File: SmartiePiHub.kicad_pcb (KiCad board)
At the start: 2 copper layers, 65 x 56 mm, 10 parts, among them P1 Conn_02x20_Odd_Even

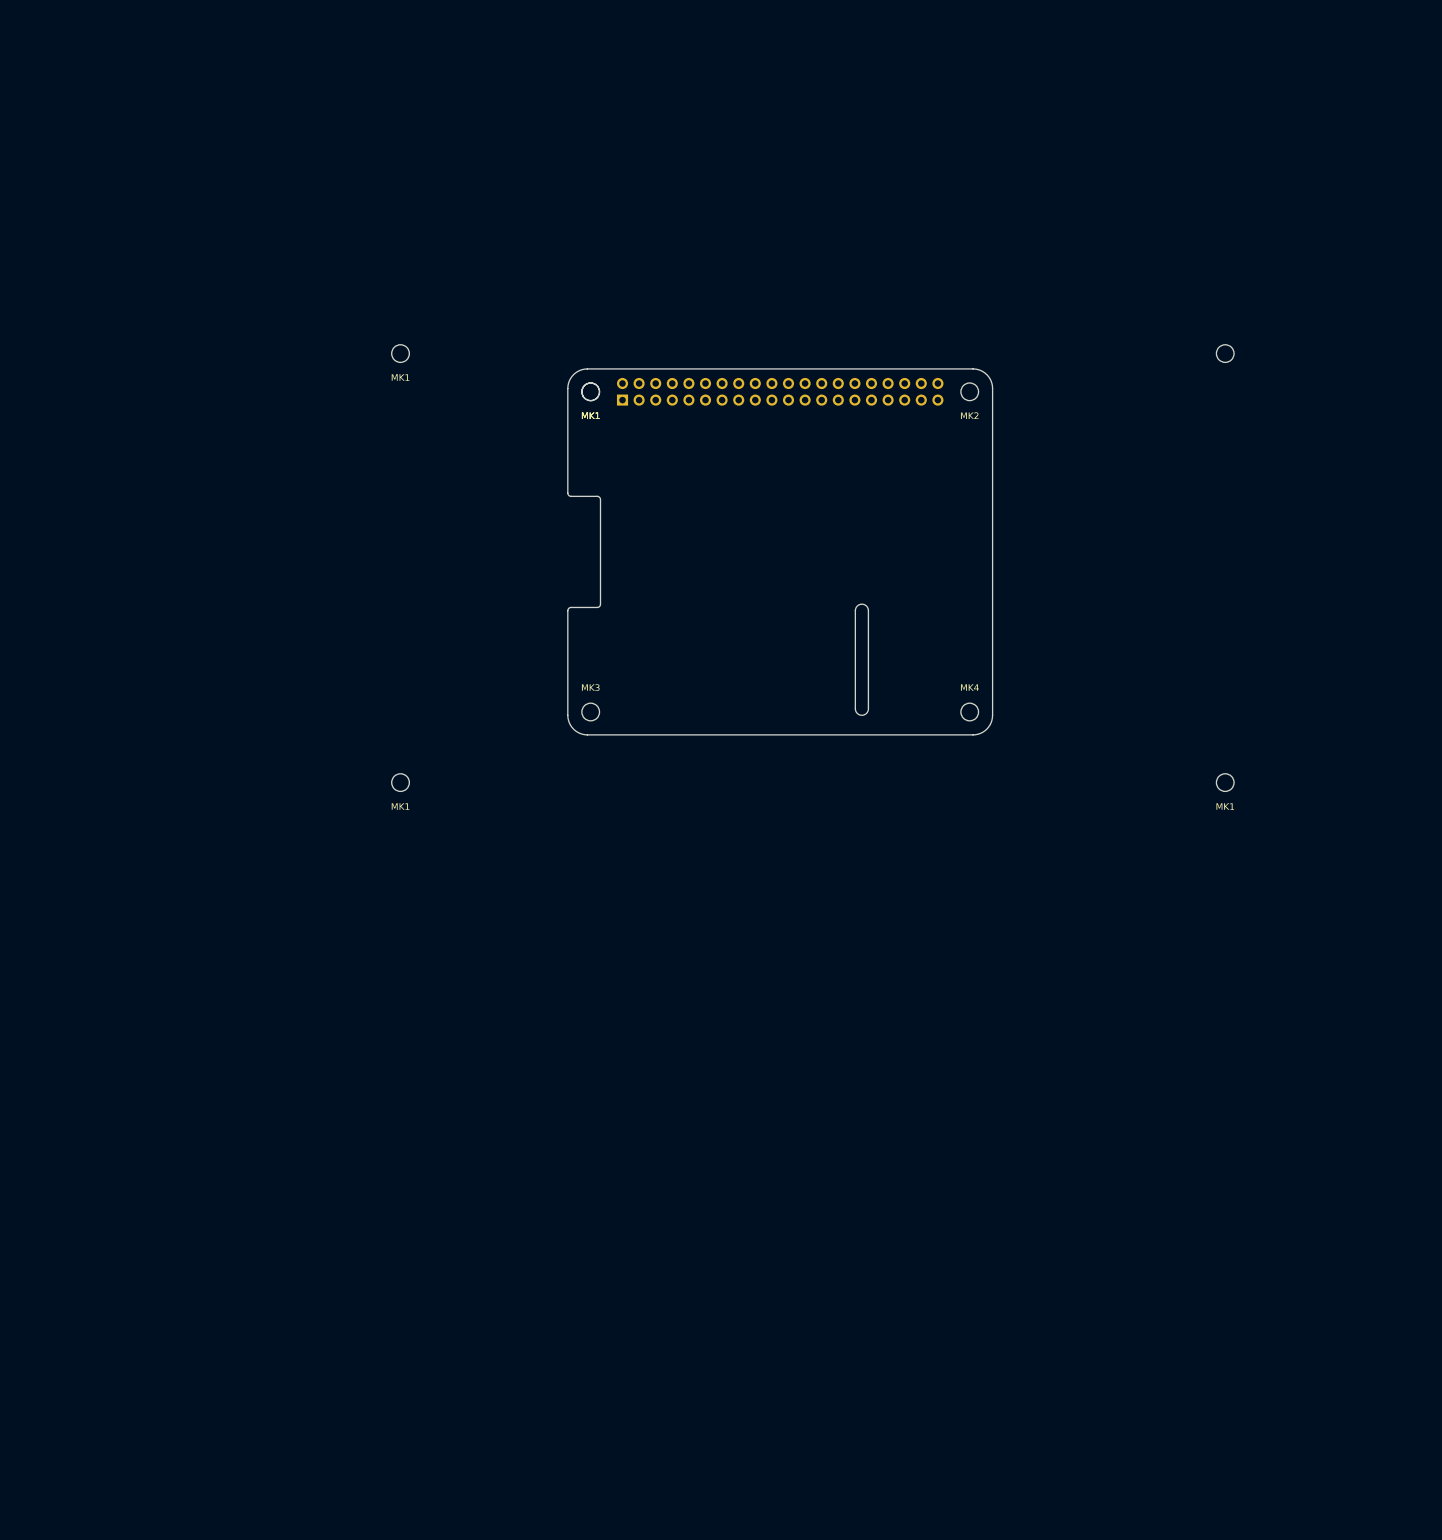
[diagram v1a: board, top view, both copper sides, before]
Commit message: adding more footprints. created netlist
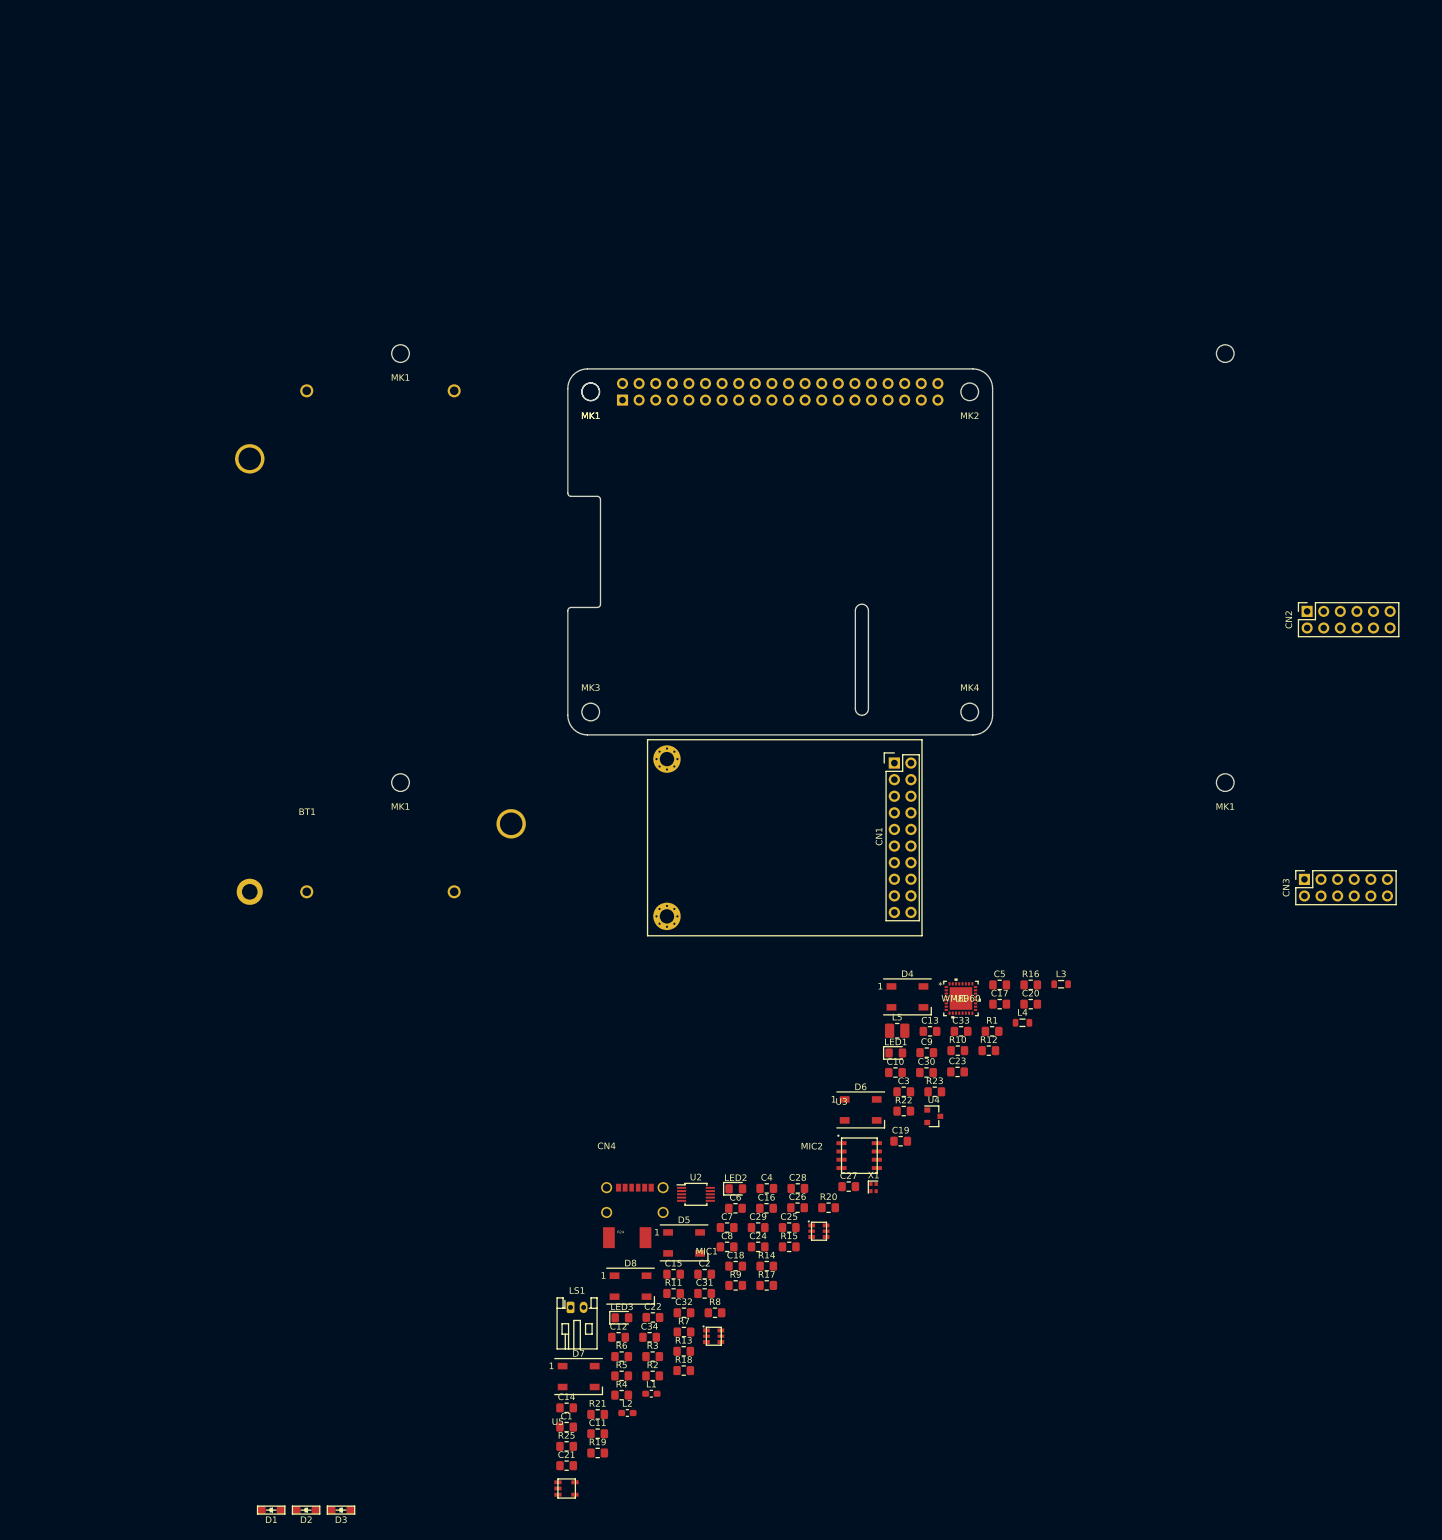
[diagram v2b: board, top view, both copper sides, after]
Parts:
- added BT1: Battery_Cell, SmartiePiHub:KEYSTONE_1123_BATTERY_HOLDER, F.Cu at (160.1, 174.0)
- added C1: 10uF, Capacitor_SMD:C_0805_2012Metric_Pad1.15x1.40mm_HandSolder, F.Cu at (199.8, 255.9)
- added C10: 33pF, Capacitor_SMD:C_0805_2012Metric_Pad1.15x1.40mm_HandSolder, F.Cu at (250.1, 201.7)
- added C11: 33pF, Capacitor_SMD:C_0805_2012Metric_Pad1.15x1.40mm_HandSolder, F.Cu at (204.6, 256.9)
- added C12: 100nF, Capacitor_SMD:C_0805_2012Metric_Pad1.15x1.40mm_HandSolder, F.Cu at (207.8, 242.2)
- added C13: 33pF, Capacitor_SMD:C_0805_2012Metric_Pad1.15x1.40mm_HandSolder, F.Cu at (255.4, 195.4)
- added C14: 33pF, Capacitor_SMD:C_0805_2012Metric_Pad1.15x1.40mm_HandSolder, F.Cu at (199.8, 253.0)
- added C15: 10uF, Capacitor_SMD:C_0805_2012Metric_Pad1.15x1.40mm_HandSolder, F.Cu at (216.2, 232.5)
- added C16: 10uF, Capacitor_SMD:C_0805_2012Metric_Pad1.15x1.40mm_HandSolder, F.Cu at (230.4, 222.4)
- added C17: 10uF, Capacitor_SMD:C_0805_2012Metric_Pad1.15x1.40mm_HandSolder, F.Cu at (266.1, 191.2)
- added C18: .1uF, Capacitor_SMD:C_0805_2012Metric_Pad1.15x1.40mm_HandSolder, F.Cu at (225.7, 231.3)
- added C19: 10uF, Capacitor_SMD:C_0805_2012Metric_Pad1.15x1.40mm_HandSolder, F.Cu at (250.9, 212.2)
- added C2: 10uF, Capacitor_SMD:C_0805_2012Metric_Pad1.15x1.40mm_HandSolder, F.Cu at (220.9, 232.5)
- added C20: .1uF, Capacitor_SMD:C_0805_2012Metric_Pad1.15x1.40mm_HandSolder, F.Cu at (270.8, 191.2)
- added C21: 100pF, Capacitor_SMD:C_0805_2012Metric_Pad1.15x1.40mm_HandSolder, F.Cu at (199.8, 261.8)
- added C22: 10pF, Capacitor_SMD:C_0805_2012Metric_Pad1.15x1.40mm_HandSolder, F.Cu at (213.0, 239.1)
- added C23: DNP, Capacitor_SMD:C_0805_2012Metric_Pad1.15x1.40mm_HandSolder, F.Cu at (259.6, 201.6)
- added C24: 4.7uF, Capacitor_SMD:C_0805_2012Metric_Pad1.15x1.40mm_HandSolder, F.Cu at (229.1, 228.3)
- added C25: .1uF, Capacitor_SMD:C_0805_2012Metric_Pad1.15x1.40mm_HandSolder, F.Cu at (233.9, 225.4)
- added C26: 10uF, Capacitor_SMD:C_0805_2012Metric_Pad1.15x1.40mm_HandSolder, F.Cu at (235.2, 222.4)
- added C27: 10uF, Capacitor_SMD:C_0805_2012Metric_Pad1.15x1.40mm_HandSolder, F.Cu at (243.0, 219.1)
- added C28: 10uF, Capacitor_SMD:C_0805_2012Metric_Pad1.15x1.40mm_HandSolder, F.Cu at (235.2, 219.4)
- added C29: DNP, Capacitor_SMD:C_0805_2012Metric_Pad1.15x1.40mm_HandSolder, F.Cu at (229.1, 225.4)
- added C3: .1uF, Capacitor_SMD:C_0805_2012Metric_Pad1.15x1.40mm_HandSolder, F.Cu at (251.4, 204.6)
- added C30: snub cap, Capacitor_SMD:C_0805_2012Metric_Pad1.15x1.40mm_HandSolder, F.Cu at (254.9, 201.7)
- added C31: 10uF, Capacitor_SMD:C_0805_2012Metric_Pad1.15x1.40mm_HandSolder, F.Cu at (220.9, 235.5)
- added C32: 22uF, Capacitor_SMD:C_0805_2012Metric_Pad1.15x1.40mm_HandSolder, F.Cu at (217.8, 238.4)
- added C33: 10uF, Capacitor_SMD:C_0805_2012Metric_Pad1.15x1.40mm_HandSolder, F.Cu at (260.2, 195.4)
- added C34: DNP, Capacitor_SMD:C_0805_2012Metric_Pad1.15x1.40mm_HandSolder, F.Cu at (212.5, 242.2)
- added C4: .1uF, Capacitor_SMD:C_0805_2012Metric_Pad1.15x1.40mm_HandSolder, F.Cu at (230.4, 219.4)
- added C5: .1uF, Capacitor_SMD:C_0805_2012Metric_Pad1.15x1.40mm_HandSolder, F.Cu at (266.1, 188.3)
- added C6: 10uF, Capacitor_SMD:C_0805_2012Metric_Pad1.15x1.40mm_HandSolder, F.Cu at (225.7, 222.4)
- added C7: .1uF, Capacitor_SMD:C_0805_2012Metric_Pad1.15x1.40mm_HandSolder, F.Cu at (224.4, 225.4)
- added C8: 10uF, Capacitor_SMD:C_0805_2012Metric_Pad1.15x1.40mm_HandSolder, F.Cu at (224.4, 228.3)
- added C9: .1uF, Capacitor_SMD:C_0805_2012Metric_Pad1.15x1.40mm_HandSolder, F.Cu at (254.9, 198.6)
- added CN1: SX1238_TRX_HEADER, SmartiePiHub:sx1238_trx, F.Cu at (250.0, 154.3)
- added CN2: ZIGBEE_TRX_HEADER, Connector_PinSocket_2.54mm:PinSocket_2x06_P2.54mm_Vertical, F.Cu at (313.1, 131.1)
- added CN3: ZWAVE_TRX_HEADER, Connector_PinSocket_2.54mm:PinSocket_2x06_P2.54mm_Vertical, F.Cu at (312.7, 172.1)
- added CN4: USB_C_Plug_USB2.0, SmartiePiHub:USB4125_TYPE_C, F.Cu at (205.9, 219.3)
- added D1: D_Schottky, SmartiePiHub:onsemi-NRVB120VLSFT1G, F.Cu at (154.6, 268.6)
- added D2: D_Schottky, SmartiePiHub:onsemi-NRVB120VLSFT1G, F.Cu at (160.0, 268.6)
- added D3: D_Schottky, SmartiePiHub:onsemi-NRVB120VLSFT1G, F.Cu at (165.3, 268.6)
- added D4: WS2812B, LED_SMD:LED_WS2812B_PLCC4_5.0x5.0mm_P3.2mm, F.Cu at (252.0, 190.1)
- added D5: WS2812B, LED_SMD:LED_WS2812B_PLCC4_5.0x5.0mm_P3.2mm, F.Cu at (217.8, 227.7)
- added D6: WS2812B, LED_SMD:LED_WS2812B_PLCC4_5.0x5.0mm_P3.2mm, F.Cu at (244.8, 207.4)
- added D7: WS2812B, LED_SMD:LED_WS2812B_PLCC4_5.0x5.0mm_P3.2mm, F.Cu at (201.7, 248.2)
- added D8: WS2812B, LED_SMD:LED_WS2812B_PLCC4_5.0x5.0mm_P3.2mm, F.Cu at (209.6, 234.4)
- added L1: BLM18BD252SN1, Inductor_SMD:L_0603_1608Metric_Pad1.05x0.95mm_HandSolder, F.Cu at (212.8, 250.8)
- added L2: BLM18BD252SN1, Inductor_SMD:L_0603_1608Metric_Pad1.05x0.95mm_HandSolder, F.Cu at (209.1, 253.8)
- added L3: 120R, Inductor_SMD:L_0805_2012Metric, F.Cu at (275.5, 188.2)
- added L4: 120R, Inductor_SMD:L_0805_2012Metric, F.Cu at (269.6, 194.1)
- added L5: 2.2uH, Inductor_SMD:L_1008_2520Metric_Pad1.43x2.20mm_HandSolder, F.Cu at (250.4, 195.3)
- added LED1: DNP, LED_SMD:LED_0805_2012Metric_Pad1.15x1.40mm_HandSolder, F.Cu at (250.2, 198.7)
- added LED2: DNP, LED_SMD:LED_0805_2012Metric_Pad1.15x1.40mm_HandSolder, F.Cu at (225.7, 219.5)
- added LED3: RED, LED_SMD:LED_0805_2012Metric_Pad1.15x1.40mm_HandSolder, F.Cu at (208.3, 239.2)
- added LS1: Speaker, Connector_JST:JST_PH_S2B-PH-K_1x02_P2.00mm_Horizontal, F.Cu at (200.4, 237.6)
- added MIC1: SPH1642HT5H_MIC, SmartiePiHub:SPH1642HT5H, F.Cu at (221.2, 241.1)
- added MIC2: SPH1642HT5H_MIC, SmartiePiHub:SPH1642HT5H, F.Cu at (237.3, 225.1)
- added R1: 10, Resistor_SMD:R_0805_2012Metric_Pad1.15x1.40mm_HandSolder, F.Cu at (264.9, 195.4)
- added R10: 10K, Resistor_SMD:R_0805_2012Metric_Pad1.15x1.40mm_HandSolder, F.Cu at (259.7, 198.3)
- added R11: DNP, Resistor_SMD:R_0805_2012Metric_Pad1.15x1.40mm_HandSolder, F.Cu at (216.2, 235.5)
- added R12: DNP, Resistor_SMD:R_0805_2012Metric_Pad1.15x1.40mm_HandSolder, F.Cu at (264.4, 198.3)
- added R13: DNP, Resistor_SMD:R_0805_2012Metric_Pad1.15x1.40mm_HandSolder, F.Cu at (217.7, 244.3)
- added R14: 10K, Resistor_SMD:R_0805_2012Metric_Pad1.15x1.40mm_HandSolder, F.Cu at (230.4, 231.3)
- added R15: 10K, Resistor_SMD:R_0805_2012Metric_Pad1.15x1.40mm_HandSolder, F.Cu at (233.9, 228.3)
- added R16: DNP, Resistor_SMD:R_0805_2012Metric_Pad1.15x1.40mm_HandSolder, F.Cu at (270.8, 188.3)
- added R17: DNP, Resistor_SMD:R_0805_2012Metric_Pad1.15x1.40mm_HandSolder, F.Cu at (230.4, 234.2)
- added R18: 1K, Resistor_SMD:R_0805_2012Metric_Pad1.15x1.40mm_HandSolder, F.Cu at (217.7, 247.3)
- added R19: 1K, Resistor_SMD:R_0805_2012Metric_Pad1.15x1.40mm_HandSolder, F.Cu at (204.6, 259.9)
- added R2: 10, Resistor_SMD:R_0805_2012Metric_Pad1.15x1.40mm_HandSolder, F.Cu at (213.0, 248.1)
- added R20: 1K, Resistor_SMD:R_0805_2012Metric_Pad1.15x1.40mm_HandSolder, F.Cu at (239.9, 222.4)
- added R21: 10K, Resistor_SMD:R_0805_2012Metric_Pad1.15x1.40mm_HandSolder, F.Cu at (204.6, 254.0)
- added R22: snub res, Resistor_SMD:R_0805_2012Metric_Pad1.15x1.40mm_HandSolder, F.Cu at (251.4, 207.6)
- added R23: 150K, Resistor_SMD:R_0805_2012Metric_Pad1.15x1.40mm_HandSolder, F.Cu at (256.2, 204.6)
- added R24: 0.1/1% (PT2512FK-070R1L), SmartiePiHub:2512, F.Cu at (209.1, 226.9)
- added R25: 0, Resistor_SMD:R_0805_2012Metric_Pad1.15x1.40mm_HandSolder, F.Cu at (199.8, 258.9)
- added R3: 10, Resistor_SMD:R_0805_2012Metric_Pad1.15x1.40mm_HandSolder, F.Cu at (213.0, 245.1)
- added R4: 10, Resistor_SMD:R_0805_2012Metric_Pad1.15x1.40mm_HandSolder, F.Cu at (208.2, 251.0)
- added R5: 10, Resistor_SMD:R_0805_2012Metric_Pad1.15x1.40mm_HandSolder, F.Cu at (208.2, 248.1)
- added R6: 10K, Resistor_SMD:R_0805_2012Metric_Pad1.15x1.40mm_HandSolder, F.Cu at (208.2, 245.1)
- added R7: 10K, Resistor_SMD:R_0805_2012Metric_Pad1.15x1.40mm_HandSolder, F.Cu at (217.8, 241.4)
- added R8: DNP, Resistor_SMD:R_0805_2012Metric_Pad1.15x1.40mm_HandSolder, F.Cu at (222.5, 238.4)
- added R9: 10K, Resistor_SMD:R_0805_2012Metric_Pad1.15x1.40mm_HandSolder, F.Cu at (225.7, 234.2)
- added U1: WM8960, SmartiePiHub:WM8960CGEFL&slash_V, F.Cu at (260.2, 190.3)
- added U2: MCP73833T-AMMF, Package_SO:MSOP-10_3x3mm_P0.5mm, F.Cu at (219.6, 220.3)
- added U3: INA219, SmartiePiHub:INA219_SOIC_8, F.Cu at (241.9, 212.5)
- added U4: XC6206_3.3V, Package_TO_SOT_SMD:SOT-23, F.Cu at (256.0, 208.4)
- added U5: TPS613222A, SmartiePiHub:TPS613222_SOT23_5, F.Cu at (198.5, 264.4)
- added X1: ASDAIG_24MHz, Oscillator:Oscillator_SMD_Abracon_ASCO-4Pin_1.6x1.2mm, F.Cu at (246.8, 219.3)

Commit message: 3d models
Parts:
- moved MIC1 193.7 mm to (324.1, 77.0)
- moved D7 193.4 mm to (297.2, 80.1)
- moved MIC2 170.7 mm to (151.3, 77.5)
- moved D8 160.1 mm to (179.7, 77.1)
- moved D5 158.2 mm to (273.7, 79.8)
- moved CN4 131.0 mm to (325.4, 165.7), turned to 90 degrees
- moved D6 129.5 mm to (241.2, 78.0)
- moved D4 120.2 mm to (210.2, 77.4)
- moved CN2 117.7 mm to (204.6, 176.5), turned to 180 degrees
- moved CN3 58.7 mm to (254.2, 176.6), turned to 180 degrees
- moved CN1 46.3 mm to (293.9, 139.7), turned to 180 degrees
- moved BT1 2.82 mm to (157.4, 175.1)

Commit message: updating pcb placement
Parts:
- moved MIC1 227.7 mm to (118.0, 174.1), turned to 180 degrees
- moved CN4 207.0 mm to (119.8, 142.7), turned to 270 degrees
- moved MK1 172.9 mm to (141.5, 159.4), turned to 0 degrees
- moved MK1 171.3 mm to (141.5, 93.8), turned to 0 degrees
- moved LS1 166.3 mm to (236.0, 75.2), turned to 180 degrees
- moved BT1 149.7 mm to (287.0, 100.0), turned to 180 degrees
- moved CN1 147.8 mm to (148.2, 114.9), turned to 270 degrees
- moved MIC2 137.3 mm to (288.6, 78.3), turned to 180 degrees
- moved CN3 123.5 mm to (179.9, 77.9), turned to 0 degrees
- moved MK1 115.3 mm to (267.7, 159.4), turned to 0 degrees
- moved MK1 112.9 mm to (267.7, 93.8), turned to 0 degrees
- moved CN2 101.6 mm to (223.5, 76.7), turned to 0 degrees
- moved MK2 98.4 mm to (180.6, 153.6), turned to 0 degrees
- moved MK4 91.1 mm to (180.6, 104.6), turned to 180 degrees
- moved MK1 66.1 mm to (238.6, 153.6), turned to 0 degrees
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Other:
- outline, holes or cut-outs redrawn
- board text removed: "RASPBERRY-PI 40-PIN ADDON BOARD VIEW FROM TOP NOTE: P1 SHOULD BE FITTED ON THE REVERSE OF THE BOARD ADD EDGE CUTS FROM CAMERA AND DISPLAY PORTS AS REQUIRED"
